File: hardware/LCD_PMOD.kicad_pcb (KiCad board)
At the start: 2 copper layers, 175.3 x 95.2 mm, 154 parts, among them IC1 TPS61169DCKR, IC2 TPD4E001DRLR, IC3 AR1021-I/SS, IC4 M24C32-WMN6P, J1 20-pin power socket, J10 OS0, J11 OS1, J12 OS2, J13 PAR, J14 RANGE, J15 REF, J16 TBA1E, J17 FTDI, J2 VS_SCL, J3 28-pin module socket, J4 691327310016, J5 691327310016, J6 HS_SDA, J7 JMP_A0, J8 DE_IRQ, J9 DIB_V2, U1 ADS8586S, U2 REF5025AD, U3 DS90CF364AMTD, U4 DS90CF36B, U6 THS4032ID, U7 THS4551IDGKT, U8 THS4551IDGKT

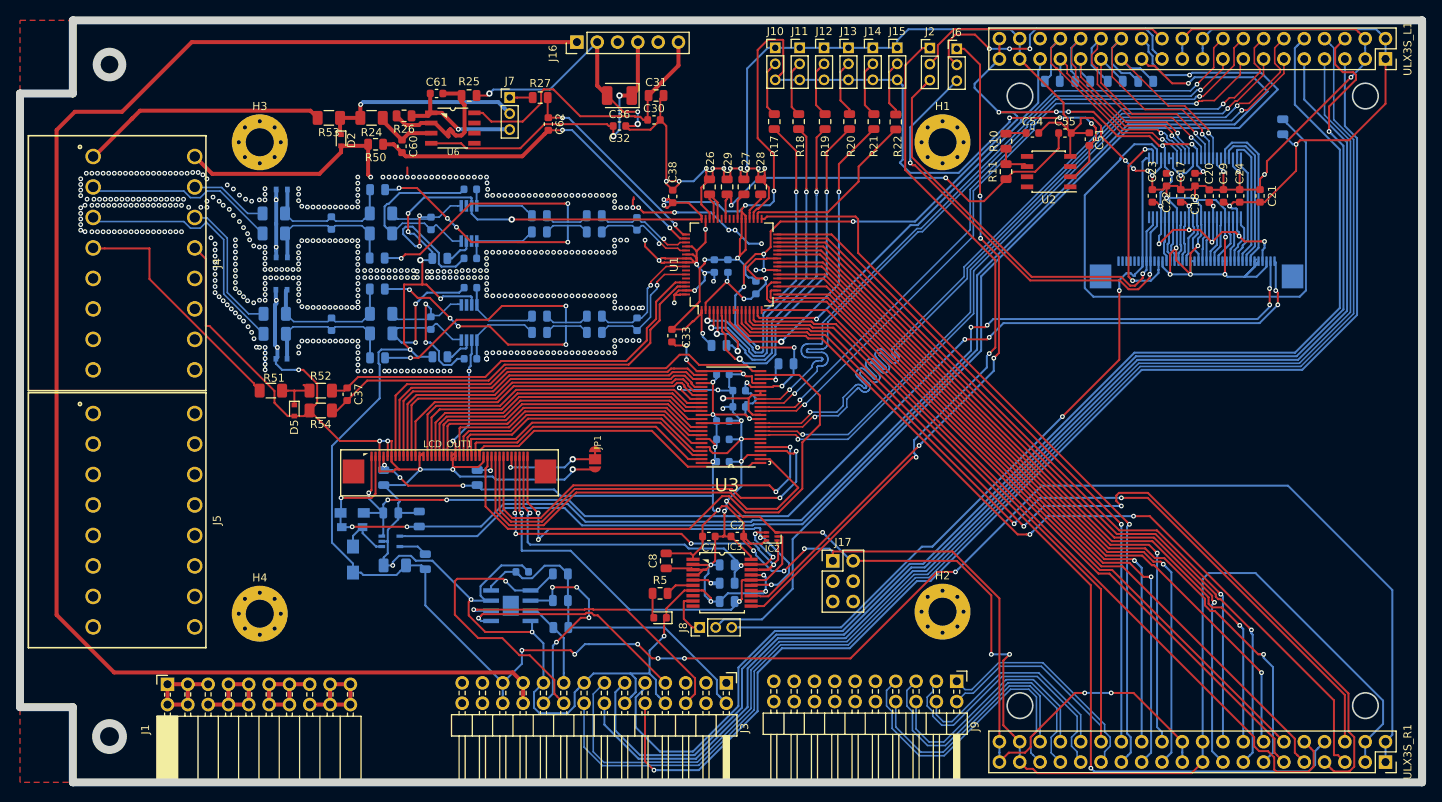
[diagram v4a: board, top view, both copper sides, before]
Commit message: Before AGND - GND
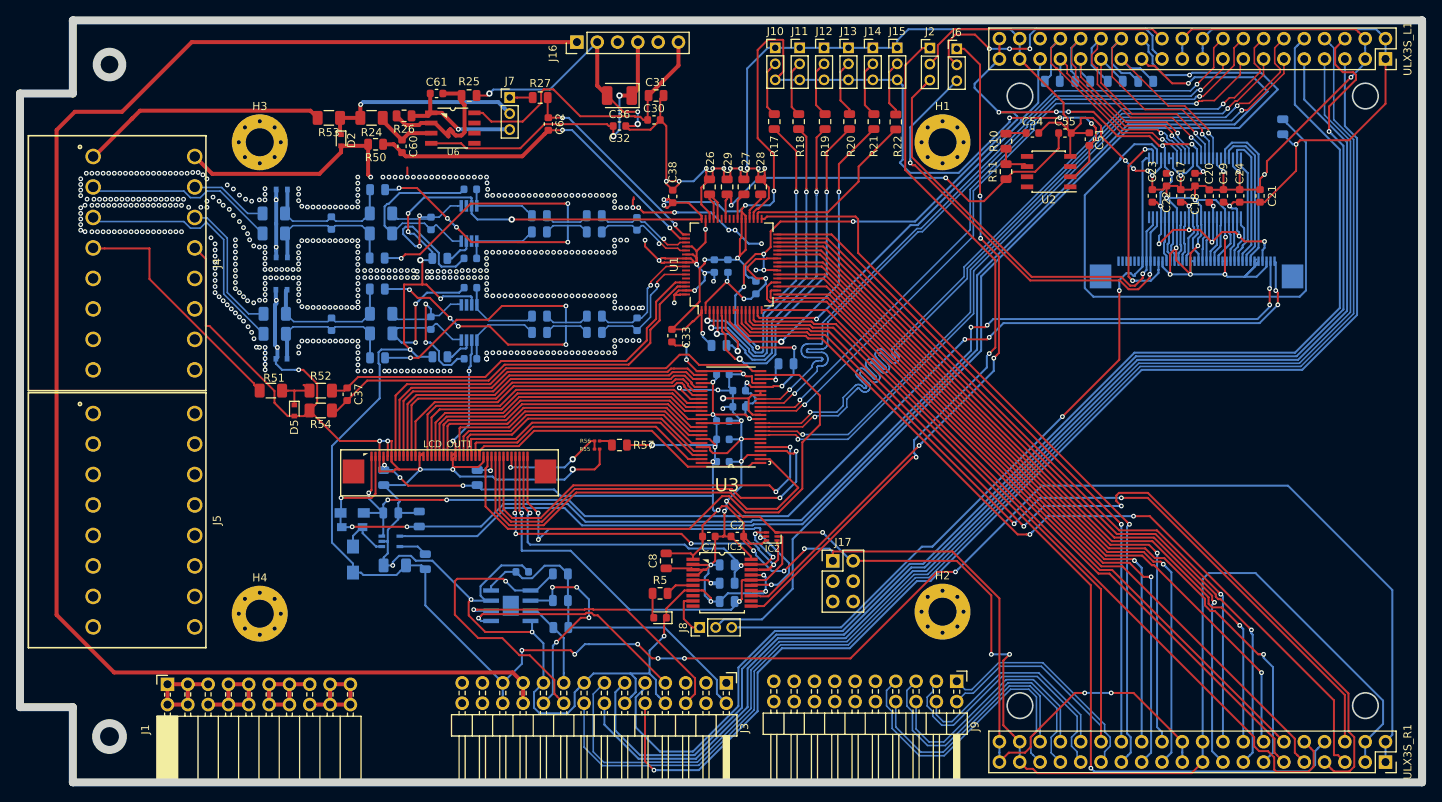
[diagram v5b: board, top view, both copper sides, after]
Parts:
- removed JP1: JP3-CUT, EEZ DIB MCU r1B1:JP3-CUT
- added R55: R0, Resistor_SMD:R_0201_0603Metric, F.Cu at (130.0, 94.0)
- added R56: R0, Resistor_SMD:R_0201_0603Metric, F.Cu at (130.0, 93.0)
- added R57: 10K, Resistor_SMD:R_0805_2012Metric, F.Cu at (132.8, 93.5)
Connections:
- net /LCD/LTDC_CLK renamed LTDC_CLK
- net /LCD/LTDC_DE renamed LTDC_DE
- net /LCD/LTDC_HSYNC renamed LTDC_HSYNC
- net /LCD/LTDC_VSYNC renamed LTDC_VSYNC
- net /Video_IN/CLK_IN renamed STM32_CLK_IN
- C1 pad 2: ADC_REFGND -> ADC_A4GND
- C10 pad 2: ADC_REFGND -> ADC_A4GND
- C11 pad 2: ADC_REFGND -> ADC_A4GND
- C12 pad 2: ADC_REFGND -> ADC_A4GND
- C13 pad 2: ADC_REFGND -> ADC_A4GND
- C14 pad 2: ADC_REFGND -> ADC_A4GND
- C17 pad 2: ADC_REFGND -> ADC_A4GND
- C18 pad 2: ADC_REFGND -> ADC_A4GND
- C19 pad 2: ADC_REFGND -> ADC_A4GND
- C2 pad 1: ADC_REFGND -> ADC_A4GND
- C20 pad 2: ADC_REFGND -> ADC_A4GND
- C21 pad 2: ADC_REFGND -> ADC_A4GND
- C22 pad 2: ADC_REFGND -> ADC_A4GND
- C23 pad 2: ADC_REFGND -> ADC_A4GND
- C24 pad 2: ADC_REFGND -> ADC_A4GND
- C25 pad 1: ADC_REFGND -> ADC_A4GND
- C26 pad 2: ADC_REFGND -> ADC_A4GND
- C27 pad 1: ADC_REFGND -> ADC_A4GND
- C28 pad 1: ADC_REFGND -> ADC_A4GND
- C29 pad 2: ADC_REFGND -> ADC_A4GND
- C3 pad 2: ADC_REFGND -> ADC_A4GND
- C30 pad 2: ADC_REFGND -> ADC_A4GND
- C31 pad 2: ADC_REFGND -> ADC_A4GND
- C32 pad 2: ADC_REFGND -> ADC_A4GND
- C33 pad 2: ADC_REFGND -> ADC_A4GND
- C34 pad 2: ADC_REFGND -> ADC_A4GND
- C35 pad 2: ADC_REFGND -> ADC_A4GND
- C36 pad 2: ADC_REFGND -> ADC_A4GND
- C38 pad 2: ADC_REFGND -> ADC_A4GND
- C39 pad 2: ADC_REFGND -> ADC_A4GND
- C4 pad 2: ADC_REFGND -> ADC_A4GND
- C5 pad 2: ADC_REFGND -> ADC_A4GND
- C51 pad 2: ADC_REFGND -> ADC_A4GND
- C54 pad 2: ADC_REFGND -> ADC_A4GND
- C55 pad 2: ADC_REFGND -> ADC_A4GND
- C6 pad 2: ADC_REFGND -> ADC_A4GND
- C7 pad 1: ADC_REFGND -> ADC_A4GND
- C8 pad 1: ADC_REFGND -> ADC_A4GND
- C9 pad 2: ADC_REFGND -> ADC_A4GND
- D2 pad 2: ADC_REFGND -> ADC_A4GND
- D3 pad 2: ADC_REFGND -> ADC_A4GND
- D4 pad 2: ADC_REFGND -> ADC_A4GND
- D5 pad 2: ADC_REFGND -> ADC_A4GND
- D6 pad 2: ADC_REFGND -> ADC_A4GND
- D7 pad 2: ADC_REFGND -> ADC_A4GND
- H1 pad 1: Net-(H1-Pad1) -> ADC_A4GND
- H2 pad 1: Net-(H2-Pad1) -> ADC_A4GND
- H3 pad 1: Net-(H3-Pad1) -> ADC_A4GND
- H4 pad 1: Net-(H4-Pad1) -> ADC_A4GND
- IC1 pad 2: ADC_REFGND -> ADC_A4GND
- IC2 pad 3: ADC_REFGND -> ADC_A4GND
- IC3 pad 14: ADC_REFGND -> ADC_A4GND
- IC3 pad 17: ADC_REFGND -> ADC_A4GND
- IC3 pad 2: ADC_REFGND -> ADC_A4GND
- IC3 pad 20: ADC_REFGND -> ADC_A4GND
- IC3 pad 3: ADC_REFGND -> ADC_A4GND
- IC3 pad 4: ADC_REFGND -> ADC_A4GND
- IC3 pad 7: ADC_REFGND -> ADC_A4GND
- IC4 pad 4: ADC_REFGND -> ADC_A4GND
- IC4 pad 7: ADC_REFGND -> ADC_A4GND
- J10 pad 1: ADC_REFGND -> ADC_A4GND
- J11 pad 1: ADC_REFGND -> ADC_A4GND
- J12 pad 1: ADC_REFGND -> ADC_A4GND
- J13 pad 1: ADC_REFGND -> ADC_A4GND
- J14 pad 1: ADC_REFGND -> ADC_A4GND
- J15 pad 1: ADC_REFGND -> ADC_A4GND
- J16 pad 2: ADC_REFGND -> ADC_A4GND
- J17 pad 2: ADC_REFGND -> ADC_A4GND
- J17 pad 3: (no net) -> 2N
- J17 pad 4: (no net) -> 1P
- J17 pad 5: (no net) -> 1N
- J17 pad 6: (no net) -> 13P
- J3 pad 12: ADC_REFGND -> ADC_A4GND
- J3 pad 15: ADC_REFGND -> ADC_A4GND
- J3 pad 19: ADC_REFGND -> ADC_A4GND
- J3 pad 25: (no net) -> 13P
- J3 pad 26: ADC_REFGND -> ADC_A4GND
- J3 pad 3: (no net) -> 13N
- J3 pad 8: ADC_REFGND -> ADC_A4GND
- J4 pad 12: ADC_REFGND -> ADC_A4GND
- J4 pad 9: ADC_REFGND -> ADC_A4GND
- LCD_IN1 pad 13: ADC_REFGND -> ADC_A4GND
- LCD_IN1 pad 14: ADC_REFGND -> ADC_A4GND
- LCD_IN1 pad 21: ADC_REFGND -> ADC_A4GND
- LCD_IN1 pad 22: ADC_REFGND -> ADC_A4GND
- LCD_IN1 pad 29: ADC_REFGND -> ADC_A4GND
- LCD_IN1 pad 3: ADC_REFGND -> ADC_A4GND
- LCD_IN1 pad 36: (no net) -> STM32_PWR_DWN
- LCD_IN1 pad 5: ADC_REFGND -> ADC_A4GND
- LCD_IN1 pad 6: ADC_REFGND -> ADC_A4GND
- LCD_OUT1 pad 13: ADC_REFGND -> ADC_A4GND
- LCD_OUT1 pad 14: ADC_REFGND -> ADC_A4GND
- LCD_OUT1 pad 21: ADC_REFGND -> ADC_A4GND
- LCD_OUT1 pad 22: ADC_REFGND -> ADC_A4GND
- LCD_OUT1 pad 29: ADC_REFGND -> ADC_A4GND
- LCD_OUT1 pad 3: ADC_REFGND -> ADC_A4GND
- LCD_OUT1 pad 5: ADC_REFGND -> ADC_A4GND
- LCD_OUT1 pad 6: ADC_REFGND -> ADC_A4GND
- R16 pad 1: Net-(R16-Pad1) -> STM32_PWR_DWN
- R2 pad 2: ADC_REFGND -> ADC_A4GND
- R25 pad 1: ADC_REFGND -> ADC_A4GND
- R50 pad 2: ADC_REFGND -> ADC_A4GND
- R54 pad 2: ADC_REFGND -> ADC_A4GND
- TOUCH1 pad 1: ADC_REFGND -> ADC_A4GND
- U1 pad 2: ADC_REFGND -> ADC_A4GND
- U1 pad 26: ADC_REFGND -> ADC_A4GND
- U1 pad 35: ADC_REFGND -> ADC_A4GND
- U1 pad 40: ADC_REFGND -> ADC_A4GND
- U1 pad 41: ADC_REFGND -> ADC_A4GND
- U1 pad 43: ADC_REFGND -> ADC_A4GND
- U1 pad 46: ADC_REFGND -> ADC_A4GND
- U1 pad 47: ADC_REFGND -> ADC_A4GND
- U1 pad 52: ADC_REFGND -> ADC_A4GND
- U1 pad 54: ADC_REFGND -> ADC_A4GND
- U1 pad 55: ADC_REFGND -> ADC_A4GND
- U1 pad 56: ADC_REFGND -> ADC_A4GND
- U1 pad 58: (no net) -> ADC_A4GND
- U1 pad 60: (no net) -> ADC_A4GND
- U1 pad 63: ADC_REFGND -> ADC_A4GND
- U1 pad 64: ADC_REFGND -> ADC_A4GND
- U2 pad 4: ADC_REFGND -> ADC_A4GND
- U3 pad 13: ADC_REFGND -> ADC_A4GND
- U3 pad 18: ADC_REFGND -> ADC_A4GND
- U3 pad 19: ADC_REFGND -> ADC_A4GND
- U3 pad 21: ADC_REFGND -> ADC_A4GND
- U3 pad 25: ADC_REFGND -> ADC_A4GND
- U3 pad 3: ADC_REFGND -> ADC_A4GND
- U3 pad 32: ADC_REFGND -> ADC_A4GND
- U3 pad 38: ADC_REFGND -> ADC_A4GND
- U3 pad 44: ADC_REFGND -> ADC_A4GND
- U3 pad 7: ADC_REFGND -> ADC_A4GND
- U4 pad 11: ADC_REFGND -> ADC_A4GND
- U4 pad 17: ADC_REFGND -> ADC_A4GND
- U4 pad 24: ADC_REFGND -> ADC_A4GND
- U4 pad 27: Net-(R16-Pad1) -> STM32_PWR_DWN
- U4 pad 28: ADC_REFGND -> ADC_A4GND
- U4 pad 30: ADC_REFGND -> ADC_A4GND
- U4 pad 31: ADC_REFGND -> ADC_A4GND
- U4 pad 36: ADC_REFGND -> ADC_A4GND
- U4 pad 42: ADC_REFGND -> ADC_A4GND
- U4 pad 46: ADC_REFGND -> ADC_A4GND
- U4 pad 5: ADC_REFGND -> ADC_A4GND
- U7 pad 6: ADC_REFGND -> ADC_A4GND
- U8 pad 6: ADC_REFGND -> ADC_A4GND
- ULX3S_L1 pad 21: ADC_REFGND -> ADC_A4GND
- ULX3S_L1 pad 22: ADC_REFGND -> ADC_A4GND
- ULX3S_L1 pad 3: ADC_REFGND -> ADC_A4GND
- ULX3S_L1 pad 36: (no net) -> 13P
- ULX3S_L1 pad 37: ADC_REFGND -> ADC_A4GND
- ULX3S_L1 pad 38: ADC_REFGND -> ADC_A4GND
- ULX3S_L1 pad 4: ADC_REFGND -> ADC_A4GND
- ULX3S_R1 pad 19: ADC_REFGND -> ADC_A4GND
- ULX3S_R1 pad 20: ADC_REFGND -> ADC_A4GND
- ULX3S_R1 pad 3: ADC_REFGND -> ADC_A4GND
- ULX3S_R1 pad 37: ADC_REFGND -> ADC_A4GND
- ULX3S_R1 pad 38: ADC_REFGND -> ADC_A4GND
- ULX3S_R1 pad 4: ADC_REFGND -> ADC_A4GND
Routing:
- net ADC_A4GND: track 0.00 -> 930.6 mm, vias 0 -> 77
- net ADC_REFGND: track 927.9 -> 0.00 mm, vias 77 -> 0
- net STM32_PWR_DWN: track 0.00 -> 75.8 mm
- net Net-(R16-Pad1): track 75.8 -> 0.00 mm
- net 3V3: track 427.9 -> 439.0 mm, vias 40 -> 41
- net /LCD/LTDC_RESET: track 12.6 -> 14.5 mm
- net Net-(R56-Pad2): track 0.00 -> 1.75 mm
- removed copper zone on F.Cu, net ADC_REFGND

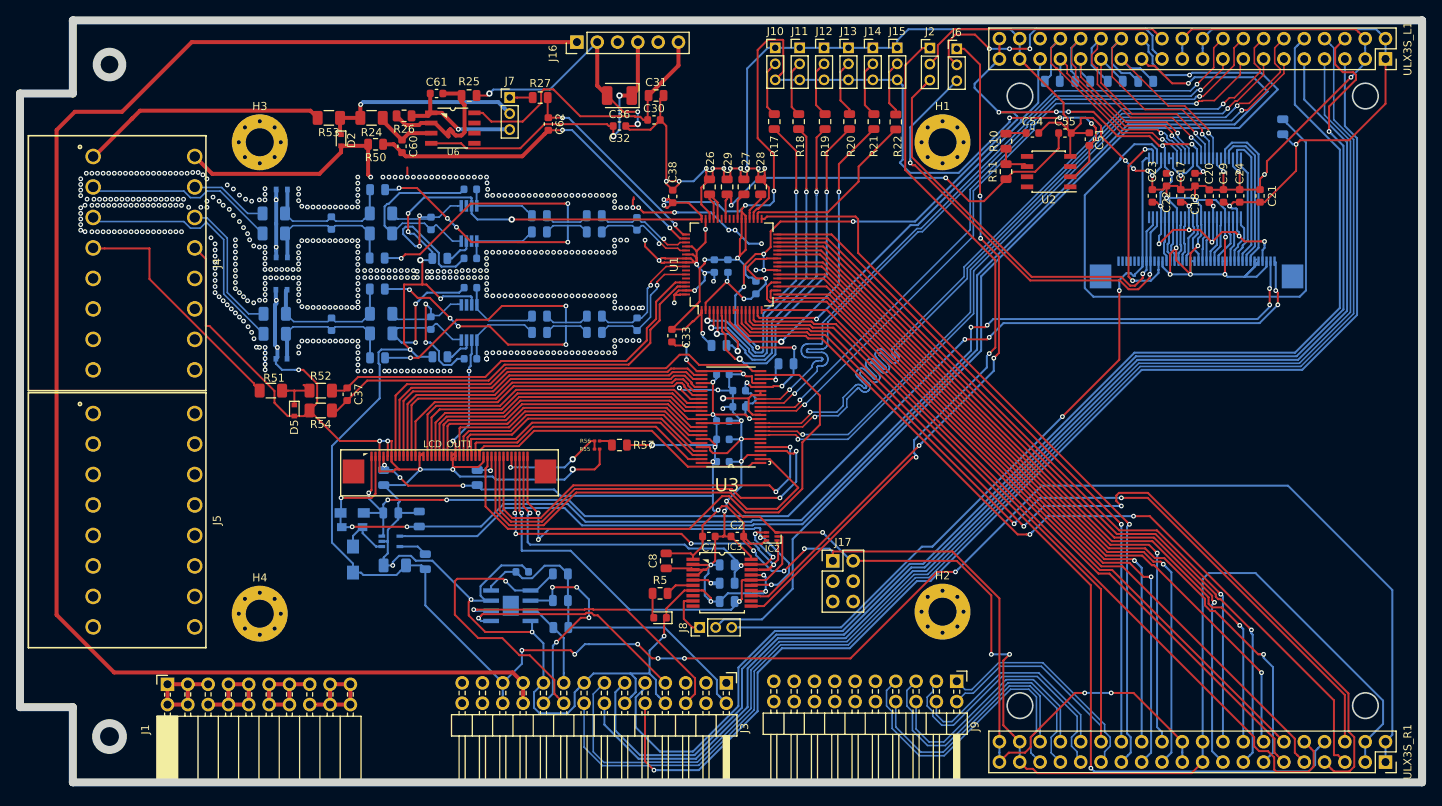
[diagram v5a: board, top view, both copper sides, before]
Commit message: Finishing routing
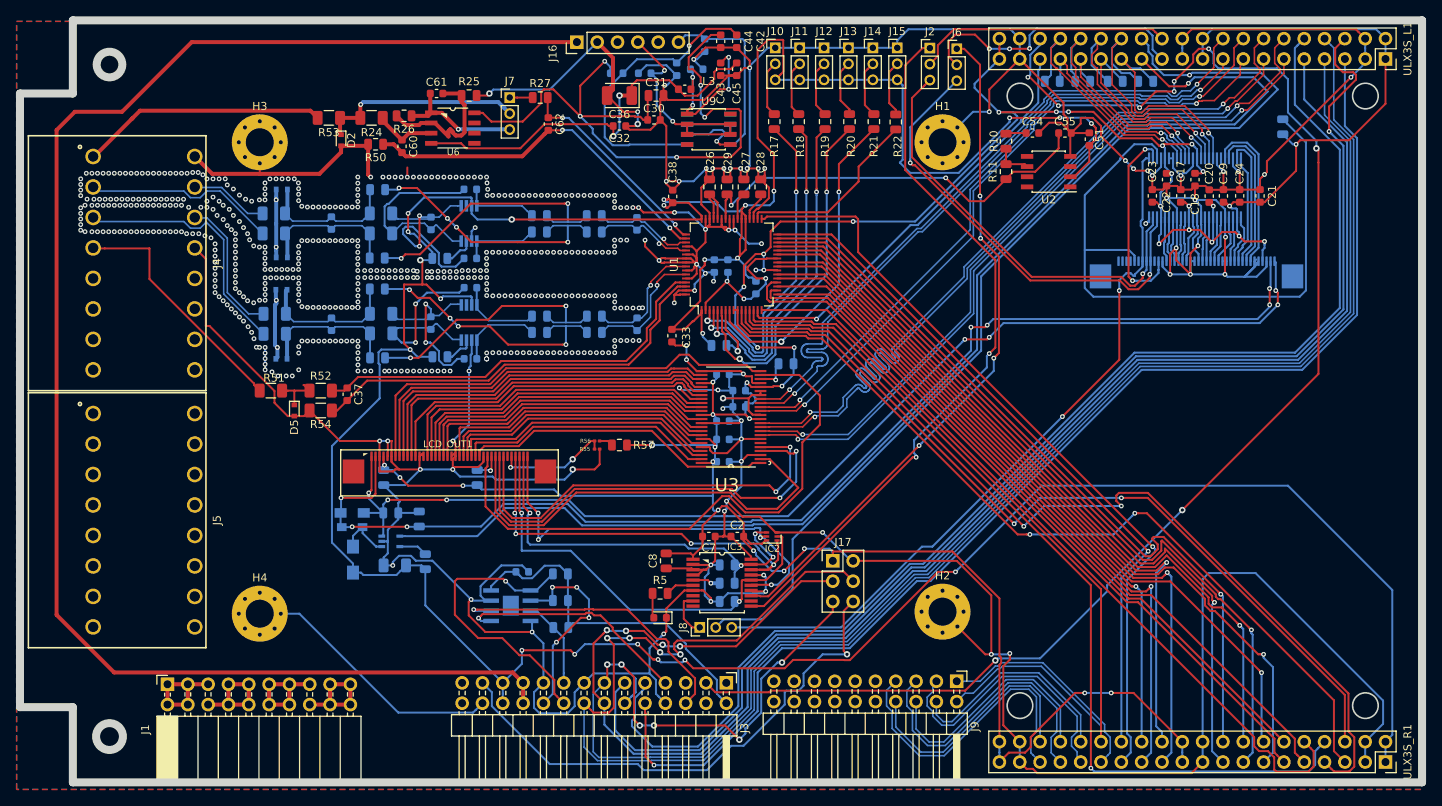
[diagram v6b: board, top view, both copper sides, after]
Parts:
- added C15: 330n, Capacitor_SMD:C_0603_1608Metric, B.Cu at (143.5, 43.5)
- added C16: 330n, Capacitor_SMD:C_0603_1608Metric, B.Cu at (136.0, 47.0)
- added C40: 100n, Capacitor_SMD:C_0603_1608Metric, B.Cu at (140.0, 46.5)
- added C41: 100n, Capacitor_SMD:C_0603_1608Metric, B.Cu at (142.5, 46.5)
- added C42: 10u, Capacitor_SMD:C_0603_1608Metric, F.Cu at (147.5, 43.0)
- added C43: 10u, Capacitor_SMD:C_0603_1608Metric, F.Cu at (145.5, 46.5)
- added C44: 10u, Capacitor_SMD:C_0603_1608Metric, F.Cu at (145.5, 43.0)
- added C45: 10u, Capacitor_SMD:C_0603_1608Metric, F.Cu at (147.5, 46.5)
- added L2: L, Capacitor_SMD:C_0603_1608Metric, B.Cu at (132.5, 47.0)
- added L3: L, Capacitor_SMD:C_0603_1608Metric, F.Cu at (141.0, 49.0)
- added U5: MC78L05_SO8, Package_SO:SOIC-8_3.9x4.9mm_P1.27mm, B.Cu at (144.0, 54.0)
- added U9: MC79L05_SO8, Package_SO:SOIC-8_3.9x4.9mm_P1.27mm, F.Cu at (144.0, 54.0)
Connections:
- net ADC_A4GND renamed GND
- J16 pad 4: HVSS -> HVSS_9V
- J16 pad 6: HVDD -> HVDD_9V
- J17 pad 6: 13P -> DIB_BOOT
- J3 pad 25: 13P -> DIB_BOOT
- J3 pad 3: 13N -> 13P
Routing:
- net 13P: track 0.00 -> 178.6 mm, vias 0 -> 9
- net GND: track 930.6 -> 1054.2 mm, vias 77 -> 556
- net DIB_BOOT: track 0.00 -> 66.2 mm, vias 0 -> 1
- net 1P: track 164.8 -> 216.0 mm, vias 0 -> 4
- net HVDD: track 37.5 -> 85.6 mm, vias 0 -> 5
- net 1N: track 163.5 -> 211.4 mm, vias 0 -> 6
- net 2N: track 157.0 -> 199.3 mm, vias 0 -> 4
- net Net-(C40-Pad1): track 0.00 -> 37.3 mm, vias 0 -> 1
- net HVSS_9V: track 0.00 -> 29.2 mm, vias 0 -> 2
- net AGND: track 23.3 -> 0.00 mm, vias 449 -> 0
- net HVDD_9V: track 0.00 -> 22.9 mm
- net Net-(C41-Pad1): track 0.00 -> 19.4 mm, vias 0 -> 4
- net Net-(U5-Pad2): track 0.00 -> 17.7 mm, vias 0 -> 1
- net HVSS: track 39.6 -> 50.2 mm
- net STM32_PWR_DWN: track 75.8 -> 83.0 mm
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- added copper zone on B.Cu, net GND
- added copper zone on F.Cu, net GND

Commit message: Adding pcb changes to PBC
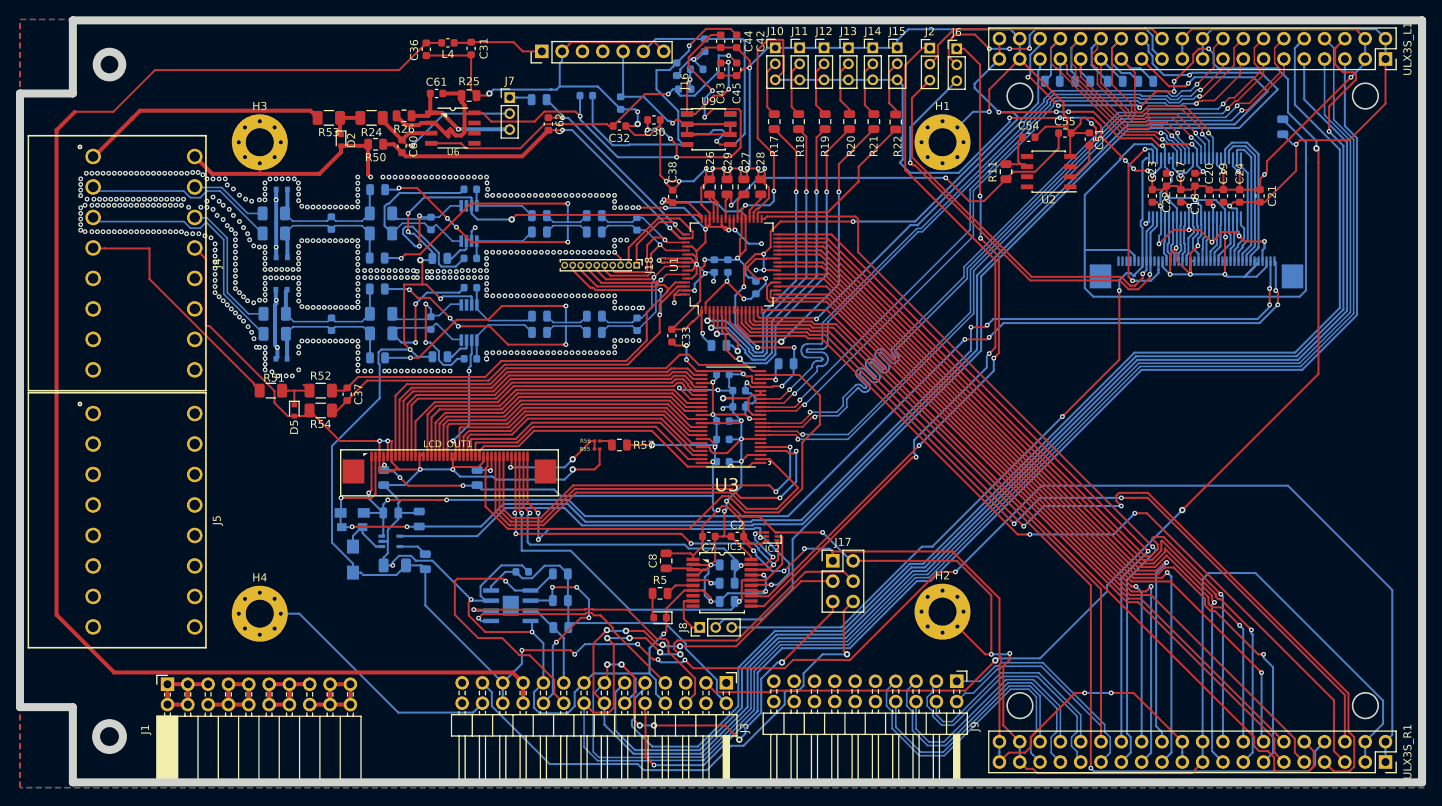
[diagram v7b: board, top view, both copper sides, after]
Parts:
- removed R10: 0,22R, Resistor_SMD:R_0805_2012Metric
- added J18: Conn_01x10, Connector_PinHeader_1.00mm:PinHeader_1x10_P1.00mm_Vertical, F.Cu at (135.0, 71.0)
- added L4: 6.8uF, Resistor_SMD:R_0603_1608Metric, F.Cu at (111.4, 43.2)
- C30, C32: value 100n -> 2.2u
- C31: value CP -> 4.7u; footprint Capacitor_SMD:C_0805_2012Metric -> Capacitor_SMD:C_0603_1608Metric
- C36: value CP -> 4.7u; footprint Capacitor_Tantalum_SMD:CP_EIA-3528-21_Kemet-B -> Capacitor_SMD:C_0603_1608Metric
- J16: value TBA1E -> MDD01; footprint TBA1E:TBA1E -> MDS01:MDS01
- L3, R27: moved to B.Cu
- moved C36 24.8 mm to (108.7, 44.0), turned to 270 degrees
- moved C31 23.9 mm to (114.3, 43.9), turned to 270 degrees
- moved J16 9.03 mm to (137.0, 47.8), turned to 270 degrees
- moved C16 4.78 mm to (133.0, 50.7), turned to 270 degrees
- moved L2 4.72 mm to (128.7, 49.8)
- moved C54 0.70 mm to (184.0, 55.0)
- moved R27 0.30 mm to (122.8, 50.3)
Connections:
- C31 pad 1: HVDD -> Net-(C31-Pad1)
- C36 pad 1: HVSS -> +12V
- J16 pad 1: +12V -> Net-(C31-Pad1)
- J16 pad 4: HVSS_9V -> (no net)
- J16 pad 5: (no net) -> HVSS_9V
- J7 pad 2: Net-(D2-Pad1) -> Net-(C60-Pad1)
- R11 pad 2: Net-(R10-Pad1) -> Net-(C54-Pad1)
- U2 pad 6: Net-(R10-Pad1) -> Net-(C54-Pad1)
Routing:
- net Net-(D2-Pad1): track 25.7 -> 4.68 mm, vias 1 -> 0
- net +12V: track 194.6 -> 177.6 mm
- net ADC_A1GND: track 45.5 -> 62.0 mm
- net ADC_A6GND: track 52.8 -> 68.5 mm, vias 0 -> 2
- net Net-(C60-Pad1): track 7.77 -> 23.1 mm, vias 0 -> 1
- net HVDD: track 85.6 -> 71.1 mm, vias 5 -> 6
- net ADC_A6P: track 52.0 -> 64.7 mm
- net Net-(C31-Pad1): track 0.00 -> 11.5 mm
- net ADC_A2_OUT_P: track 12.8 -> 23.4 mm
- net ADC_A4_OUT_N: track 16.1 -> 26.4 mm
- net ADC_A2_OUT_N: track 12.8 -> 22.9 mm
- net ADC_A1P: track 26.0 -> 35.3 mm
- net ADC_A4_OUT_P: track 15.7 -> 24.2 mm
- net Net-(C54-Pad1): track 2.55 -> 7.37 mm
- net Net-(R10-Pad1): track 4.69 -> 0.00 mm
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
